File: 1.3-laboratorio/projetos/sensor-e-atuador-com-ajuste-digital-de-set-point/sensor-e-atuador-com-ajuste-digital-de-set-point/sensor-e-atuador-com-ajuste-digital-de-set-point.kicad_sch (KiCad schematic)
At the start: 48 parts, among them J1 Conn_01x02, J2 Conn_01x01, P1 47k, SW1 SW_PUSH, U1 LM324N, U2 4093, U3 4518, U4 CD4511BE, U5 KCSC02-105

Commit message: Versão preliminar do projeto.
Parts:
- P1: symbol Device:R_Potentiometer -> Device:R_Potentiometer_Trim
- R14: value 100k -> 220k
- R15: value 100k -> 120k
- R16: value 82k -> 160k
- R21, R22, R23, R24, R25, R26, R27: value 220R -> 1k
- SW1: symbol DD_CMOS-rescue:SW_PUSH -> Switch:SW_Push
- gave numbers to parts that had none: 6
- renumbered C4 to C7, C5 to C8
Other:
- note added: "11,3V"
- note removed: "Botão e "deboucing""
- company: (none) -> ETE103 - Fundamentos de Circuitos Analógicos
- title: (none) -> Sensor com Ajuste Digital de Set-Point para Atuador
- moved on the sheet: C3, C4, C5, C6, J2, LDR1, R1, R10, R11, R12, R13, R14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

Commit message: Alinhamentos e textos explicativos no esquemático.
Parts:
- added unit 2 of U3
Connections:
- net A: now also U3.3 (Q1), U4.7 (A)
- net B: now also U3.4 (Q2), U4.1 (B)
- net C: now also U3.5 (Q3), U4.2 (C)
- net D: now also U3.6 (Q4), U4.6 (D)
- net ck: now reaches U2.3, U3.1 (CK)
- net POR: now reaches U2.4, U3.7 (Reset)
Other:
- note added: "Amplificador Inversor com Deslocamento"
- note added: "Amplificador Subtrator"
- note added: "Comparador com Histerese"
- note added: "Entrada de Alimentação"
- note added: "Filtros"
- note added: "Partes não utilizadas"
- note added: "Ponte de Wheatstone"
- note added: "Ponto de Distribuição de Alimentação"
- note added: "Proteção contra Inversão de Polaridade"
- note added: "Rede R-2R (Conversor Digital-Analógico)"
- note removed: "POR"
- moved on the sheet: C1, C2, C3, C4, C5, C6, D1, J1, U1D, U1E, U2E, U3C

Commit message: Teste em protoboard realizado e ajustes realizados no esquemático. Projeto concluído.
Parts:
- added D2: LED_Filled, symbol Device:LED_Filled
- added J3: Conn_01x01, symbol Connector_Generic:Conn_01x01
- added P2: 47k, symbol Device:R_Potentiometer_Trim
- added R28: 1k, symbol Device:R
- added unit 3 of U2
- added unit 4 of U2
- C3, C4, C5, C6: symbol DD_CMOS-rescue:C -> Device:C
- C7, C8: symbol DD_CMOS-rescue:CP1-Device -> Device:C_Polarized_US
- LDR1: symbol ldr-ponte-rescue:R_PHOTO-Device -> Device:R_Photo
- R16: value 160k -> 120k
- R17: value 10k -> 15k
- R18: value 10k -> 100k
- R19, R20, R21, R22, R23, R24, R25, R26, R27: symbol DD_CMOS-rescue:R -> Device:R
- U5: value KCSC02-105 -> SM42056-1
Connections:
- net A: now also R6.2; no longer R12.2
- net B: now also R8.2; no longer R10.2
- net C: now also R10.2; no longer R8.2
- net D: now also R12.2; no longer R6.2
- net Earth: now also U3.10 (Enable), U3.15 (Reset), U3.9 (CK), D2.1 (K), U2.12, U2.13, U2.8, U2.9
- net Vref: now also P2.1, P2.2; no longer R16.2
- net Vs: now reaches J2.1 (Pin_1), R18.2, U1.8
- new net: P2.3, R16.2
- new net: D2.2 (A), R28.1
- new net: J3.1 (Pin_1), R28.2
- no-connect marks 2 -> 8
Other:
- note added: "(LSB)"
- note added: "(MSB)"
- note added: "1"
- note added: "10"
- note added: "5"
- note added: "6"
- note added: "Ajustar P1 de forma a comutar a saída Vs à ocorrência do menor escurecimento desejado, com o "set-point" em 0 (zero). (Sugestão: P1 = ~22kΩ.)"
- note added: "Ajuste Digital do "Set-Point""
- note added: "Alternativamente ao uso do módulo "Atuador e Carga", pode-se ligar um LED para visualizar o estado da saída."
- note added: "Amplificador (Subtrator)"
- note added: "Depois de ajustar P1, ajustar P2 de forma a comutar a saída Vs à ocorrência do maior escurecimento desejado, com o "set-point" em 9 (nove). (Sugestão: P2 = ~37kΩ.)"
- note added: "Numeração da pinagem do "display"."
- note removed: "Amplificador Inversor com Deslocamento"
- note removed: "Amplificador Subtrator"
- moved on the sheet: C7, C8, J2, R16, R19, R20, R21, R22, R23, R24, R25, R26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

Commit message: Roteiro sobre Comparadores elaborado. Atualizações do projeto Sensor e Atuador com Ajuste Digital de Set-Point.
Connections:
- net Earth: now also U1.12 (+); no longer U1.13 (-), U2.12, U2.13, U2.8, U2.9
- net VCC: now also U2.12, U2.13, U2.8, U2.9; no longer U1.12 (+)
- net at U1.14: now also U1.13 (-)

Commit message: Provas. Simulações e gráficos. Gráfico com histerese. Redimensionamento e reposicionamento de janela com gráficos: ver arquivo .cir.
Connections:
- net Vcomp: now reaches R17.2, R18.1, U1.10 (+)
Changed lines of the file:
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@@
   (title_block
     (title "Sensor com Ajuste Digital de Set-Point para Atuador")
-    (date "2022-10-11")
-    (rev "0.0.2")
+    (date "2022-10-20")
+    (rev "0.0.3")
     (company "ETE103 - Fundamentos de Circuitos Analógicos")
     (comment 1 "Licença: CC-BY-SA (https://creativecommons.org/licenses/by-sa/4.0/)")
@@
     (effects (font (size 1.27 1.27) (thickness 0.254) bold) (justify left bottom))
   )
+  (label "Vcomp" (at 233.68 83.82 180)
+    (effects (font (size 1.27 1.27)) (justify right bottom))
+  )
   (label "Vref" (at 220.98 90.17 180)

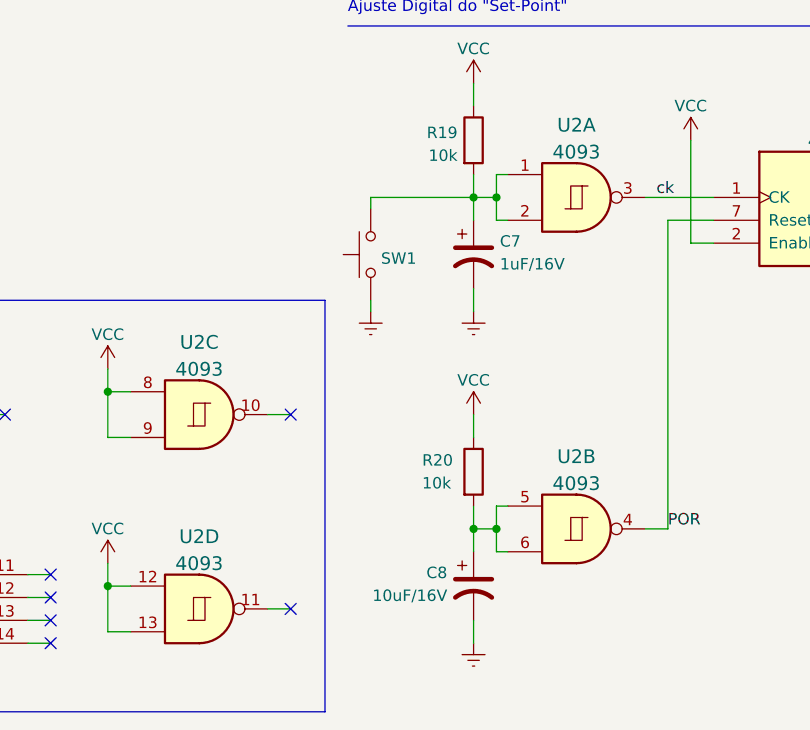
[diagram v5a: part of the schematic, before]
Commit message: Sincronização. dd_cmos: atualizado símbolo do display para com CC (catodo comum). dd_cmos_didatico: nova versão mais didática, conforme requerido.
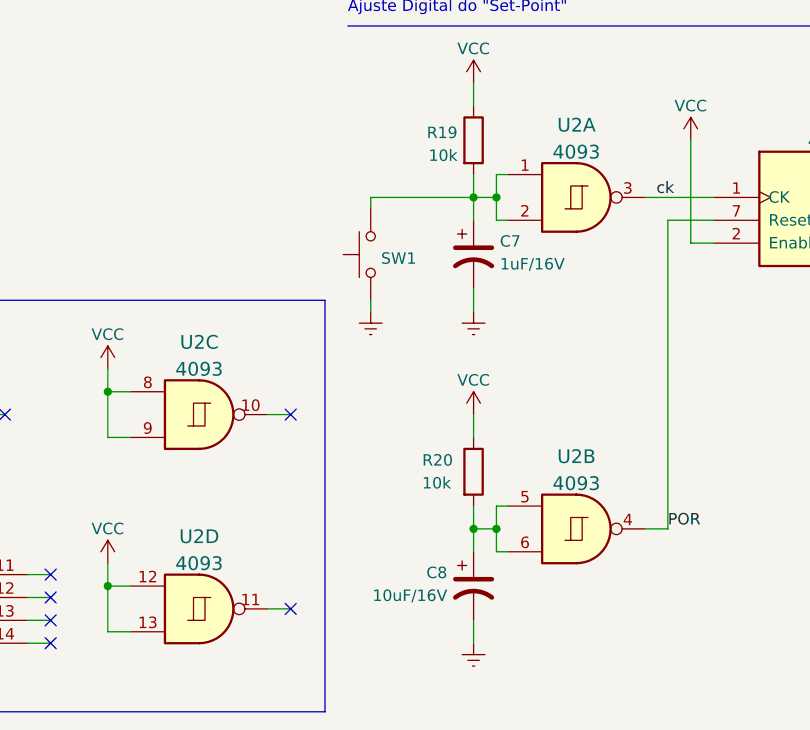
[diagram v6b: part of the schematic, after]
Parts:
- LDR1: Spice_Model 250k -> (none); Spice_Netlist_Enabled Y -> (none); Spice_Primitive R -> (none)
